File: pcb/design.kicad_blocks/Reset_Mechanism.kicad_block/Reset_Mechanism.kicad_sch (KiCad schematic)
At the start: 4 parts, among them SW1 B3U-1000P-B

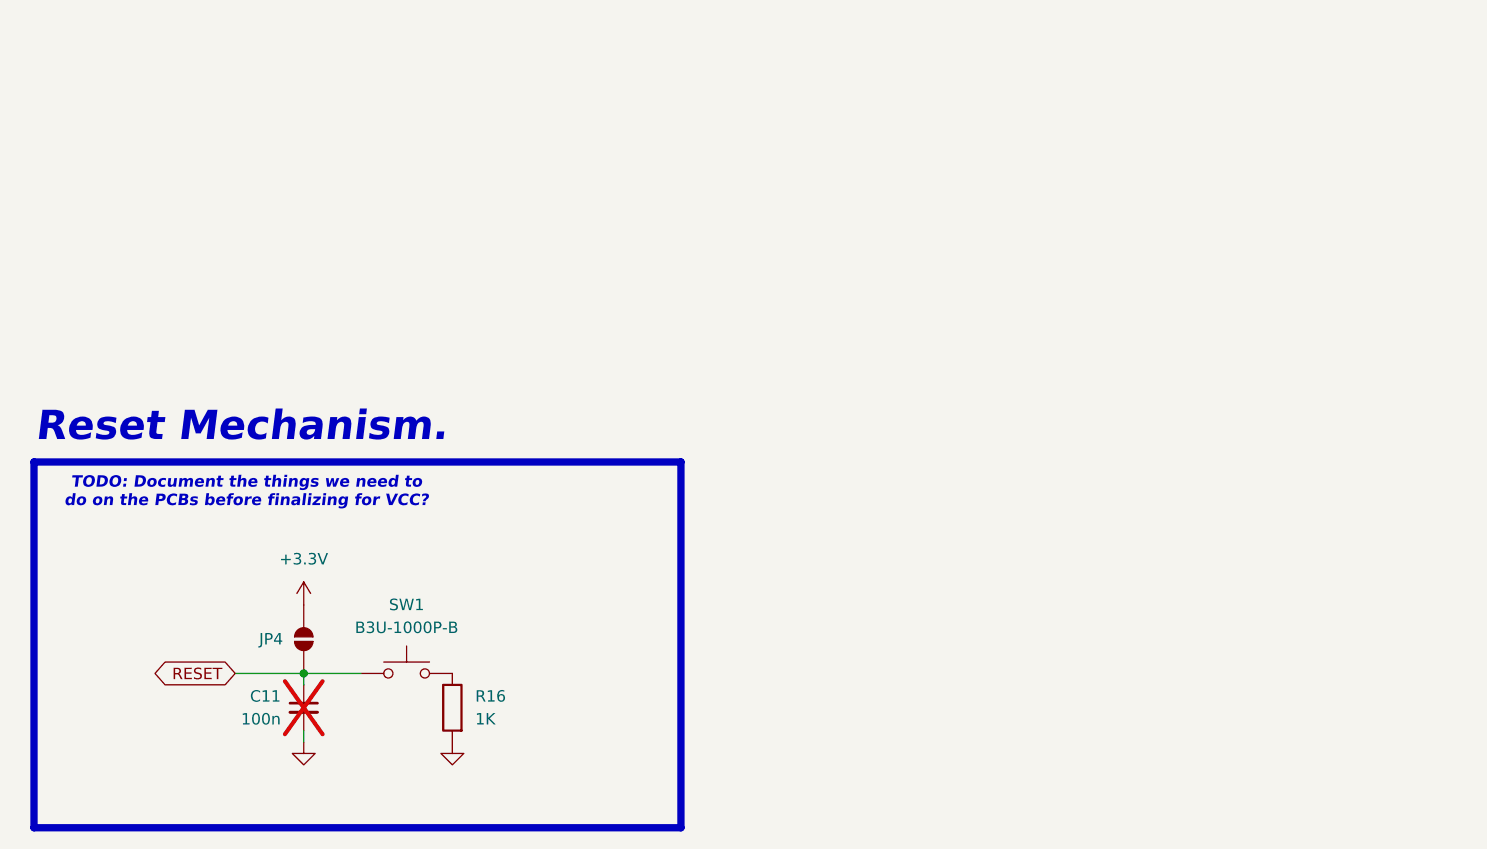
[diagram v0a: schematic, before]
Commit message: Placed down most of the components.
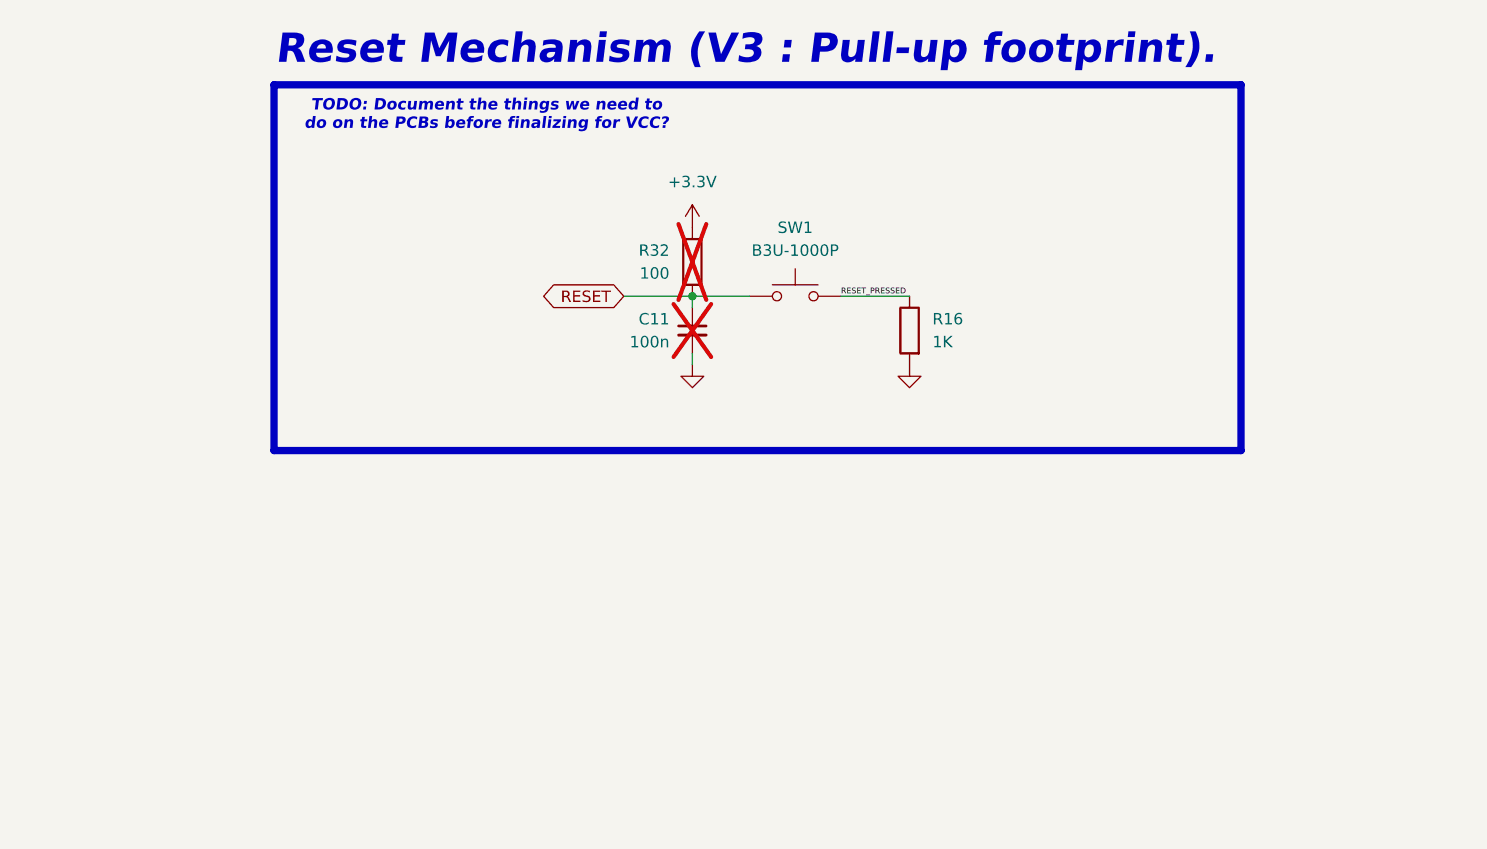
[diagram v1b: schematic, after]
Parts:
- removed JP4: SolderJumper_2_Open, Jumper:SolderJumper-2_P1.3mm_Open_RoundedPad1.0x1.5mm, symbol Jumper:SolderJumper_2_Open
- added R32: 100, Resistor_SMD:R_1206_3216Metric_Pad1.30x1.75mm_HandSolder, symbol Device:R
- SW1: value B3U-1000P-B -> B3U-1000P; footprint Button_Switch_SMD:SW_SPST_B3U-1000P-B -> Button_Switch_SMD:SW_SPST_B3U-1000P
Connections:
- net +3.3V: now also R32.1
- net RESET: now also R32.2
- net RESET_PRESSED: now reaches R16.1, SW1.2
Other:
- note added: "Reset Mechanism (V3 : Pull-up footprint)."
- note removed: "Reset Mechanism."
- moved on the sheet: C11, R16, SW1
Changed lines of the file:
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@@
 	(paper "A4")
 	(rectangle
-		(start 312.928 329.565)
-		(end 384.81 370.205)
+		(start 339.598 287.655)
+		(end 447.04 328.295)
 		(stroke
 			(width 0.8128)
@@
 		)
 	)
-	(text "Reset Mechanism."
-		(exclude_from_sim no)
-		(at 313.055 327.66 0)
+	(text "Reset Mechanism (V3 : Pull-up footprint)."
+		(exclude_from_sim no)
+		(at 339.725 285.75 0)
 		(effects
 			(font
@@
 	(text "TODO: Document the things we need to\ndo on the PCBs before finalizing for VCC?"
 		(exclude_from_sim no)
-		(at 336.55 332.994 0)
+		(at 363.22 291.084 0)
 		(effects
 			(font
@@
 	)
 	(junction
-		(at 342.9 353.06)
+		(at 386.08 311.15)
 		(diameter 0)
 		(color 0 0 0 0)
@@
 	(wire
 		(pts
-			(xy 342.9 353.06) (xy 349.25 353.06)
+			(xy 410.21 311.15) (xy 402.59 311.15)
 		)
 		(stroke
@@
 	(wire
 		(pts
-			(xy 335.28 353.06) (xy 342.9 353.06)
+			(xy 386.08 311.15) (xy 392.43 311.15)
 		)
 		(stroke
@@
 	(wire
 		(pts
-			(xy 342.9 353.06) (xy 342.9 354.33)
+			(xy 378.46 311.15) (xy 386.08 311.15)
 		)
 		(stroke
@@
 	(wire
 		(pts
-			(xy 342.9 359.41) (xy 342.9 360.68)
+			(xy 386.08 311.15) (xy 386.08 312.42)
 		)
 		(stroke
@@
 		)
 	)
+	(wire
+		(pts
+			(xy 386.08 317.5) (xy 386.08 318.77)
+		)
+		(stroke
+			(width 0)
+			(type default)
+		)
+	)
+	(label "RESET_PRESSED"
+		(at 402.59 311.15 0)
+		(effects
+			(font
+				(size 0.635 0.635)
+			)
+			(justify left bottom)
+		)
+	)
 	(global_label "RESET"
 		(shape bidirectional)
-		(at 335.28 353.06 180)
+		(at 378.46 311.15 180)
 		(fields_autoplaced yes)
 		(effects
@@
 		)
 		(property "Intersheetrefs" "${INTERSHEET_REFS}"
-			(at 325.4384 353.06 0)
+			(at 368.6184 311.15 0)
 			(effects
 				(font
@@
 	(symbol
 		(lib_id "Device:R")
-		(at 359.41 356.87 0)
+		(at 410.21 314.96 0)
 		(mirror y)
 		(unit 1)
@@
 		(fields_autoplaced yes)
 		(property "Reference" "R16"
-			(at 361.95 355.5999 0)
+			(at 412.75 313.6899 0)
 			(effects
 				(font
@@
 		)
 		(property "Value" "1K"
-			(at 361.95 358.1399 0)
+			(at 412.75 316.2299 0)
 			(effects
 				(font
@@
 		)
 		(property "Footprint" "Resistor_SMD:R_1206_3216Metric_Pad1.30x1.75mm_HandSolder"
-			(at 361.188 356.87 90)
+			(at 411.988 314.96 90)
 			(effects
 				(font
@@
 		)
 		(property "Datasheet" "~"
-			(at 359.41 356.87 0)
+			(at 410.21 314.96 0)
 			(effects
 				(font
@@
 		)
 		(property "Description" "Resistor"
-			(at 359.41 356.87 0)
+			(at 410.21 314.96 0)
 			(effects
 				(font
@@
 	(symbol
 		(lib_id "Device:C_Small")
-		(at 342.9 356.87 0)
+		(at 386.08 314.96 0)
 		(mirror y)
 		(unit 1)
@@
 		(dnp yes)
 		(property "Reference" "C11"
-			(at 340.36 355.6062 0)
+			(at 383.54 313.6962 0)
 			(effects
 				(font
@@
 		)
 		(property "Value" "100n"
-			(at 340.36 358.1462 0)
+			(at 383.54 316.2362 0)
 			(effects
 				(font
@@
 		)
 		(property "Footprint" "Capacitor_SMD:C_1206_3216Metric_Pad1.33x1.80mm_HandSolder"
-			(at 342.9 356.87 0)
+			(at 386.08 314.96 0)
 			(effects
 				(font
@@
 		)
 		(property "Datasheet" "~"
-			(at 342.9 356.87 0)
+			(at 386.08 314.96 0)
 			(effects
 				(font
@@
 		)
 		(property "Description" "Unpolarized capacitor, small symbol"
-			(at 342.9 356.87 0)
+			(at 386.08 314.96 0)
 			(effects
 				(font
@@
 	(symbol
 		(lib_id "Switch:SW_Push")
-		(at 354.33 353.06 0)
+		(at 397.51 311.15 0)
 		(unit 1)
 		(exclude_from_sim no)
@@
 		(fields_autoplaced yes)
 		(property "Reference" "SW1"
-			(at 354.33 345.44 0)
-			(effects
-				(font
-					(size 1.27 1.27)
-				)
-			)
-		)
-		(property "Value" "B3U-1000P-B"
-			(at 354.33 347.98 0)
-			(effects
-				(font
-					(size 1.27 1.27)
-				)
-			)
-		)
-		(property "Footprint" "Button_Switch_SMD:SW_SPST_B3U-1000P-B"
-			(at 354.33 347.98 0)
+			(at 397.51 303.53 0)
+			(effects
+				(font
+					(size 1.27 1.27)
+				)
+			)
+		)
+		(property "Value" "B3U-1000P"
+			(at 397.51 306.07 0)
+			(effects
+				(font
+					(size 1.27 1.27)
+				)
+			)
+		)
+		(property "Footprint" "Button_Switch_SMD:SW_SPST_B3U-1000P"
+			(at 397.51 306.07 0)
 			(effects
 				(font
@@
 		)
 		(property "Datasheet" "~"
-			(at 354.33 347.98 0)
+			(at 397.51 306.07 0)
 			(effects
 				(font
@@
 		)
 		(property "Description" "Push button switch, generic, two pins"
-			(at 354.33 353.06 0)
+			(at 397.51 311.15 0)
 			(effects
 				(font
@@
 	(symbol
 		(lib_id "power:GND")
-		(at 342.9 360.68 0)
+		(at 386.08 318.77 0)
 		(mirror y)
 		(unit 1)
@@
 		(fields_autoplaced yes)
 		(property "Reference" "#PWR043"
-			(at 342.9 367.03 0)
+			(at 386.08 325.12 0)
 			(effects
 				(font
@@
 		)
 		(property "Value" "GND"
-			(at 342.8999 364.49 90)
+			(at 386.0799 322.58 90)
 			(effects
 				(font
@@
 		)
 		(property "Footprint" ""
-			(at 342.9 360.68 0)
+			(at 386.08 318.77 0)
 			(effects
 				(font
@@
 		)
 		(property "Datasheet" ""
-			(at 342.9 360.68 0)
+			(at 386.08 318.77 0)
 			(effects
 				(font
@@
 		)
 		(property "Description" "Power symbol creates a global label with name \"GND\" , ground"
-			(at 342.9 360.68 0)
+			(at 386.08 318.77 0)
 			(effects
 				(font
@@
 	(symbol
 		(lib_id "power:+3.3V")
-		(at 342.9 345.44 0)
+		(at 386.08 303.53 0)
 		(unit 1)
 		(exclude_from_sim no)
@@
 		(fields_autoplaced yes)
 		(property "Reference" "#PWR044"
-			(at 342.9 349.25 0)
+			(at 386.08 307.34 0)
 			(effects
 				(font
@@
 		)
 		(property "Value" "+3.3V"
-			(at 342.9 340.36 0)
+			(at 386.08 298.45 0)
 			(effects
 				(font
@@
 		)
 		(property "Footprint" ""
-			(at 342.9 345.44 0)
+			(at 386.08 303.53 0)
 			(effects
 				(font
@@
 		)
 		(property "Datasheet" ""
-			(at 342.9 345.44 0)
+			(at 386.08 303.53 0)
 			(effects
 				(font
@@
 		)
 		(property "Description" "Power symbol creates a global label with name \"+3.3V\""
-			(at 342.9 345.44 0)
+			(at 386.08 303.53 0)
 			(effects
 				(font
@@
 	)
 	(symbol
-		(lib_id "Jumper:SolderJumper_2_Open")
-		(at 342.9 349.25 90)
-		(unit 1)
-		(exclude_from_sim no)
-		(in_bom no)
-		(on_board yes)
-		(dnp no)
-		(property "Reference" "JP4"
-			(at 340.614 349.25 90)
-			(effects
-				(font
-					(size 1.27 1.27)
-				)
-				(justify left)
-			)
-		)
-		(property "Value" "SolderJumper_2_Open"
-			(at 340.36 350.5199 90)
-			(effects
-				(font
-					(size 1.27 1.27)
-				)
-				(justify left)
-				(hide yes)
-			)
-		)
-		(property "Footprint" "Jumper:SolderJumper-2_P1.3mm_Open_RoundedPad1.0x1.5mm"
-			(at 342.9 349.25 0)
+		(lib_id "Device:R")
+		(at 386.08 307.34 0)
+		(unit 1)
+		(exclude_from_sim no)
+		(in_bom yes)
+		(on_board yes)
+		(dnp yes)
+		(property "Reference" "R32"
+			(at 383.54 306.0699 0)
+			(effects
+				(font
+					(size 1.27 1.27)
+				)
+				(justify right)
+			)
+		)
+		(property "Value" "100"
+			(at 383.54 308.6099 0)
+			(effects
+				(font
+					(size 1.27 1.27)
+				)
+				(justify right)
+			)
+		)
+		(property "Footprint" "Resistor_SMD:R_1206_3216Metric_Pad1.30x1.75mm_HandSolder"
+			(at 384.302 307.34 90)
 			(effects
 				(font
@@
 		)
 		(property "Datasheet" "~"
-			(at 342.9 349.25 0)
-			(effects
-				(font
-					(size 1.27 1.27)
-				)
-				(hide yes)
-			)
-		)
-		(property "Description" "Solder Jumper, 2-pole, open"
-			(at 342.9 349.25 0)
+			(at 386.08 307.34 0)
+			(effects
+				(font
+					(size 1.27 1.27)
+				)
+				(hide yes)
+			)
+		)
+		(property "Description" "Resistor"
+			(at 386.08 307.34 0)
 			(effects
 				(font
@@
 		)
 		(instances
-			(project ""
+			(project "MainFlightComputer"
 				(path "/0a179c33-cb18-4019-99e7-0e00d41f97d6"
-					(reference "JP4")
+					(reference "R32")
 					(unit 1)
 				)
@@
 	(symbol
 		(lib_id "power:GND")
-		(at 359.41 360.68 0)
+		(at 410.21 318.77 0)
 		(mirror y)
 		(unit 1)
@@
 		(fields_autoplaced yes)
 		(property "Reference" "#PWR042"
-			(at 359.41 367.03 0)
+			(at 410.21 325.12 0)
 			(effects
 				(font
@@
 		)
 		(property "Value" "GND"
-			(at 359.4099 364.49 90)
+			(at 410.2099 322.58 90)
 			(effects
 				(font
@@
 		)
 		(property "Footprint" ""
-			(at 359.41 360.68 0)
+			(at 410.21 318.77 0)
 			(effects
 				(font
@@
 		)
 		(property "Datasheet" ""
-			(at 359.41 360.68 0)
+			(at 410.21 318.77 0)
 			(effects
 				(font
@@
 		)
 		(property "Description" "Power symbol creates a global label with name \"GND\" , ground"
-			(at 359.41 360.68 0)
-			(effects
-				(font
+			(at 410.21 318.77 0)
+			(effects
+				(font
